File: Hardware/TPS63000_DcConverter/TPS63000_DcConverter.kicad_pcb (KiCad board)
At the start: 4 copper layers, 26 x 26 mm, 16 parts, among them J2 Output, J3 Input, U2 TPS63000

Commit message: Hardware updates and cleanup
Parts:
- L1: footprint Inductor_SMD:L_APV_APH0630 -> Inductor_SMD:L_APV_APH0530
- R1: value 680Ω -> 6.8kΩ
- RV2: value 2kΩ -> 20kΩ
- moved C6 37.9 mm to (159.0, 86.0), turned to -90 degrees
- moved R3 36.4 mm to (162.0, 86.0), turned to -90 degrees
- moved C5 35.5 mm to (156.0, 86.0), turned to -90 degrees
- moved C8 28.1 mm to (149.5, 88.0), turned to -90 degrees
- moved C7 25.7 mm to (147.0, 86.0), turned to 90 degrees
- moved R1 20.9 mm to (146.8, 90.0), turned to 90 degrees
- moved RV2 17.4 mm to (143.0, 87.0), turned to 180 degrees
- moved R2 16.7 mm to (142.8, 91.0)
- moved L1 1.70 mm to (152.0, 93.0)
- moved U2 0.76 mm to (152.0, 83.7), turned to 90 degrees
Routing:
- net Net-(U2-FB): track 0.00 -> 14.4 mm, vias 0 -> 2
- net Net-(U2-EN): track 0.00 -> 11.2 mm
- net Net-(R1-Pad2): track 0.00 -> 9.31 mm
- net +3V3: track 0.00 -> 8.55 mm, vias 0 -> 3
- net GND: track 0.00 -> 4.06 mm, vias 0 -> 43
- net +5V: track 0.00 -> 3.03 mm, vias 0 -> 2
- net Net-(U2-L2): track 0.00 -> 2.29 mm, vias 0 -> 6
- net Net-(U2-L1): track 0.00 -> 2.29 mm, vias 0 -> 6
- added copper zone on In2.Cu, net +3V3
- added copper zone on In2.Cu, net +5V
- added copper zone on F.Cu, net GND
- added copper zone on In1.Cu, net GND
- added copper zone on In2.Cu, net GND
- added copper zone on In2.Cu, net Net-(U2-L1)
- added copper zone on In2.Cu, net Net-(U2-L2)
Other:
- board text added: "TPS63000 Dc Converter rev. A"

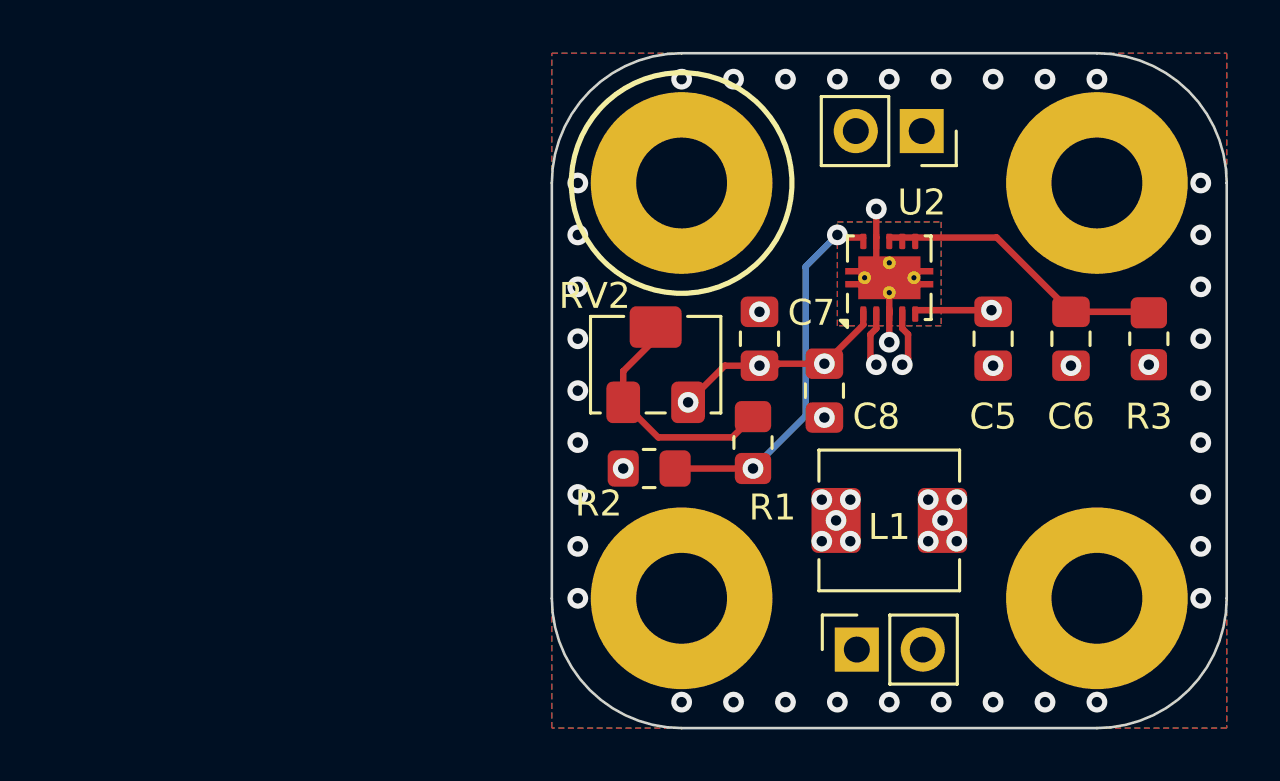
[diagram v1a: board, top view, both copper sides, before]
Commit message: Hardware updates. Add Lr04 lora module datasheets
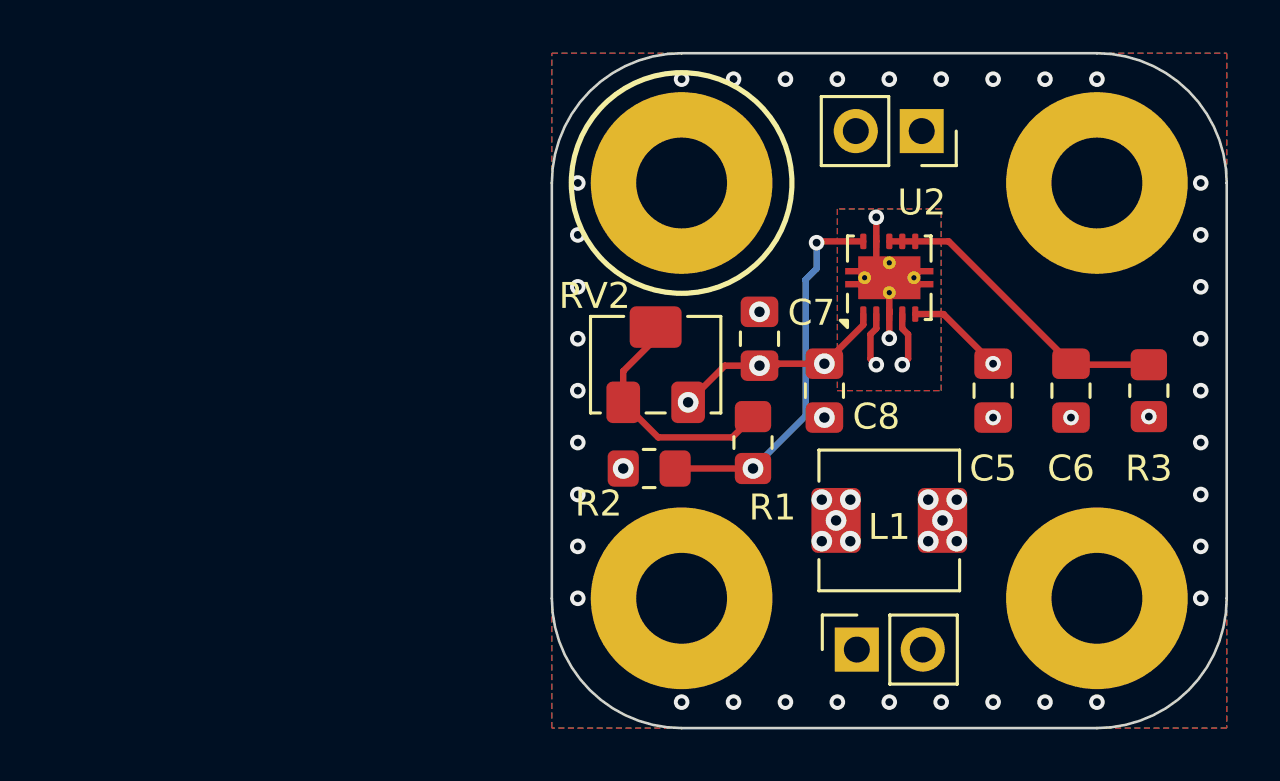
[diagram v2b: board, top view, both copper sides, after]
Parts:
- moved C5 2.00 mm to (156.0, 88.0)
- moved C6 2.00 mm to (159.0, 88.0)
- moved R3 2.00 mm to (162.0, 88.0)
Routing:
- net +5V: track 3.03 -> 3.79 mm
- net Net-(U2-EN): track 11.2 -> 12.0 mm
